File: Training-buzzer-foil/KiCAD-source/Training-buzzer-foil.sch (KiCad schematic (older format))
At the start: 13 parts, among them J1 Con, J2 DC Jack, Q1 BC547B, Q2 BC547B, Q3 BC547B

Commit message: Create PCB for foil training buzzer
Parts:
- BZ1: symbol Device:Buzzer -> Training-buzzer-foil-rescue:Buzzer-Device
- C1: symbol Device:C -> Training-buzzer-foil-rescue:C-Device
- C2: symbol Device:CP -> Training-buzzer-foil-rescue:CP-Device
- D1: symbol Device:D -> Training-buzzer-foil-rescue:D-Device
- D2: symbol Device:LED -> Training-buzzer-foil-rescue:LED-Device
- J1: symbol Connector:Conn_01x02_Male -> Training-buzzer-foil-rescue:Conn_01x02_Male-Connector
- J2: symbol Connector:Barrel_Jack_Switch -> Training-buzzer-foil-rescue:Barrel_Jack_Switch-Connector
- Q1, Q2, Q3: symbol Transistor_BJT:BC547 -> Training-buzzer-foil-rescue:BC547-Transistor_BJT
- R1, R2, R3: symbol Device:R -> Training-buzzer-foil-rescue:R-Device
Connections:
- net at Q1.1 (C), Q2.2 (B), R1.1: no longer Q1.2 (B), R2.1
- new net: Q1.2 (B), R2.1
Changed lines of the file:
@@
-EESchema Schematic File Version 5
+EESchema Schematic File Version 4
 EELAYER 30 0
 EELAYER END
@@
 Comment3 ""
 Comment4 ""
-Comment5 ""
-Comment6 ""
-Comment7 ""
-Comment8 ""
-Comment9 ""
 $EndDescr
 $Comp
-L Transistor_BJT:BC547 Q3
+L Training-buzzer-foil-rescue:BC547-Transistor_BJT Q3
 U 1 1 5DF68983
 P 5750 4350
@@
 $EndComp
 $Comp
-L Device:R R1
+L Training-buzzer-foil-rescue:R-Device R1
 U 1 1 5DF6C7EC
 P 4400 4050
@@
 	5450 4350 5450 4250
 $Comp
-L Device:D D1
+L Training-buzzer-foil-rescue:D-Device D1
 U 1 1 5DF71B05
 P 4150 3650
@@
 $EndComp
 $Comp
-L Device:Buzzer BZ1
+L Training-buzzer-foil-rescue:Buzzer-Device BZ1
 U 1 1 5DF86A1B
 P 6300 3600
@@
 $EndComp
 $Comp
-L Device:LED D2
+L Training-buzzer-foil-rescue:LED-Device D2
 U 1 1 5DF87C1E
 P 5850 3800
@@
 	5050 4650 5850 4650
 $Comp
-L Device:R R2
+L Training-buzzer-foil-rescue:R-Device R2
 U 1 1 5DF72508
 P 4650 3650
@@
 $EndComp
 $Comp
-L Transistor_BJT:BC547 Q2
+L Training-buzzer-foil-rescue:BC547-Transistor_BJT Q2
 U 1 1 5DF65CB1
 P 5350 4050
@@
 $EndComp
 $Comp
-L Transistor_BJT:BC547 Q1
+L Training-buzzer-foil-rescue:BC547-Transistor_BJT Q1
 U 1 1 5DFF3DCE
 P 4950 4350
@@
 	1    0    0    -1
 $EndComp
-Wire Wire Line
-	4550 4050 4650 4050
 Connection ~ 5050 4650
 Wire Wire Line
@@
 Connection ~ 4150 4050
 Wire Wire Line
-	4650 3800 4650 4050
-Wire Wire Line
 	4650 4350 4750 4350
 Wire Wire Line
@@
 	4650 3200 4650 3500
 $Comp
-L Device:C C1
+L Training-buzzer-foil-rescue:C-Device C1
 U 1 1 5DF7BD47
 P 4150 4350
@@
 $EndComp
 $Comp
-L Device:R R3
+L Training-buzzer-foil-rescue:R-Device R3
 U 1 1 5DF8DCED
 P 5850 3450
@@
 $EndComp
 $Comp
-L Device:CP C2
+L Training-buzzer-foil-rescue:CP-Device C2
 U 1 1 5DF9DBF4
 P 6850 3950
@@
 $EndComp
 $Comp
-L Connector:Conn_01x02_Male J1
+L Training-buzzer-foil-rescue:Conn_01x02_Male-Connector J1
 U 1 1 5DFE6D93
 P 5000 3000
@@
 	6850 3800 6850 3200
 $Comp
-L Connector:Barrel_Jack_Switch J2
+L Training-buzzer-foil-rescue:Barrel_Jack_Switch-Connector J2
 U 1 1 5DFF66BA
 P 7600 3950
@@
 Connection ~ 6850 3200
 NoConn ~ 7300 3950
-Connection ~ 4650 4050
-Wire Wire Line
-	4650 4050 5050 4050
-Wire Wire Line
-	4650 4050 4650 4350
+Wire Wire Line
+	4550 4050 5050 4050
+Wire Wire Line
+	4650 3800 4650 4350
 $EndSCHEMATC

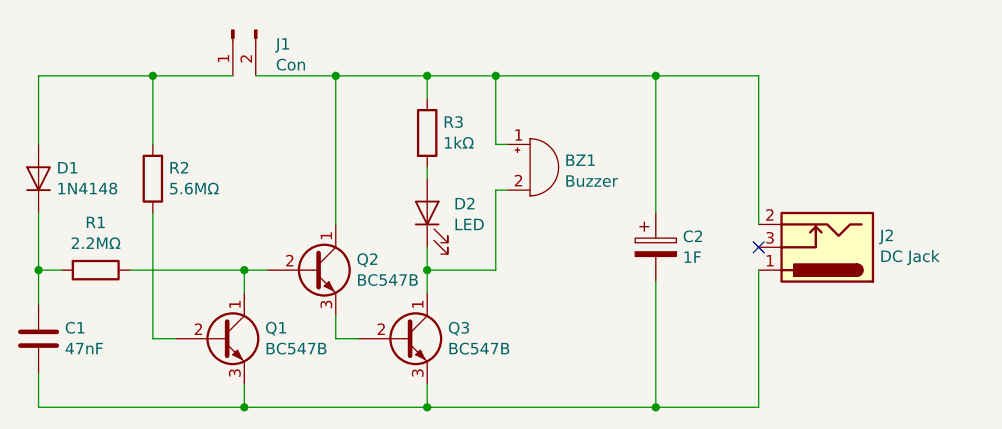
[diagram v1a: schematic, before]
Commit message: Clean up foil training buzzer schematic
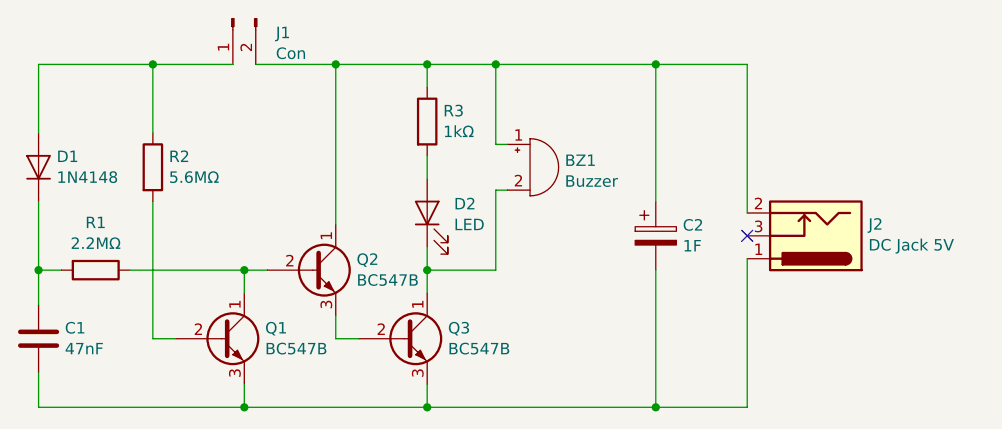
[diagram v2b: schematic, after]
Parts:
- removed BZ1: Buzzer, Buzzer_Beeper:Buzzer_12x9.5RM7.6, symbol Training-buzzer-foil-rescue:Buzzer-Device
- removed C1: 47nF, Capacitor_THT:C_Disc_D5.0mm_W2.5mm_P2.50mm, symbol Training-buzzer-foil-rescue:C-Device
- removed C2: 1F, Training-buzzer-foil:CP_Radial_Supercap_D21.5mm_P5.00mm, symbol Training-buzzer-foil-rescue:CP-Device
- removed D1: 1N4148, Diode_THT:D_A-405_P7.62mm_Horizontal, symbol Training-buzzer-foil-rescue:D-Device
- removed D2: LED, LED_THT:LED_D5.0mm_Horizontal_O1.27mm_Z15.0mm, symbol Training-buzzer-foil-rescue:LED-Device
- removed J1: Con, Training-buzzer-foil:Foil_Plug_Connector, symbol Training-buzzer-foil-rescue:Conn_01x02_Male-Connector
- removed J2: DC Jack, Connector_BarrelJack:BarrelJack_Horizontal, symbol Training-buzzer-foil-rescue:Barrel_Jack_Switch-Connector
- removed Q1, Q2, Q3: BC547B, Package_TO_SOT_THT:TO-92_Inline, symbol Training-buzzer-foil-rescue:BC547-Transistor_BJT
- removed R1: 2.2MΩ, Resistor_THT:R_Axial_DIN0207_L6.3mm_D2.5mm_P10.16mm_Horizontal, symbol Training-buzzer-foil-rescue:R-Device
- removed R2: 5.6MΩ, Resistor_THT:R_Axial_DIN0207_L6.3mm_D2.5mm_P10.16mm_Horizontal, symbol Training-buzzer-foil-rescue:R-Device
- removed R3: 1kΩ, Resistor_THT:R_Axial_DIN0207_L6.3mm_D2.5mm_P10.16mm_Horizontal, symbol Training-buzzer-foil-rescue:R-Device
- added BZ1: Buzzer, Buzzer_Beeper:Buzzer_12x9.5RM7.6, symbol Device:Buzzer
- added C1: 47nF, Capacitor_THT:C_Disc_D5.0mm_W2.5mm_P2.50mm, symbol Device:C
- added C2: 1F, Training-buzzer-foil:CP_Radial_Supercap_D21.5mm_P5.00mm, symbol Device:CP
- added D1: 1N4148, Diode_THT:D_A-405_P7.62mm_Horizontal, symbol Device:D
- added D2: LED, LED_THT:LED_D5.0mm_Horizontal_O1.27mm_Z3.0mm, symbol Device:LED
- added J1: Con, Training-buzzer-foil:Foil_Plug_Connector, symbol Connector:Conn_01x02_Male
- added J2: DC Jack 5V, Connector_BarrelJack:BarrelJack_Horizontal, symbol Connector:Barrel_Jack_Switch
- added Q1, Q2, Q3: BC547B, Package_TO_SOT_THT:TO-92_Inline, symbol Transistor_BJT:BC547
- added R1: 2.2MΩ, Resistor_THT:R_Axial_DIN0207_L6.3mm_D2.5mm_P10.16mm_Horizontal, symbol Device:R
- added R2: 5.6MΩ, Resistor_THT:R_Axial_DIN0207_L6.3mm_D2.5mm_P10.16mm_Horizontal, symbol Device:R
- added R3: 1kΩ, Resistor_THT:R_Axial_DIN0207_L6.3mm_D2.5mm_P10.16mm_Horizontal, symbol Device:R
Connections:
- new net: BZ1.2 (+), D2.1 (K), Q3.1 (C)
- new net: Q2.3 (E), Q3.2 (B)
- new net: C1.2, C2.2, J2.1, Q1.3 (E), Q3.3 (E)
- new net: BZ1.1 (-), C2.1, J1.2 (Pin_2), J2.2, Q2.1 (C), R3.1
- new net: Q1.1 (C), Q2.2 (B), R1.1
- new net: Q1.2 (B), R2.2
- new net: D1.2 (A), J1.1 (Pin_1), R2.1
- new net: D2.2 (A), R3.2
- new net: C1.1, D1.1 (K), R1.2
